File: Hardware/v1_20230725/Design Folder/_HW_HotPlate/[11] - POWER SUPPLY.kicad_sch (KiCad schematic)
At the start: 28 parts, among them U1101 MIC5528-3.3YMT-TR, U1102 MIC5528-3.3YMT-TR

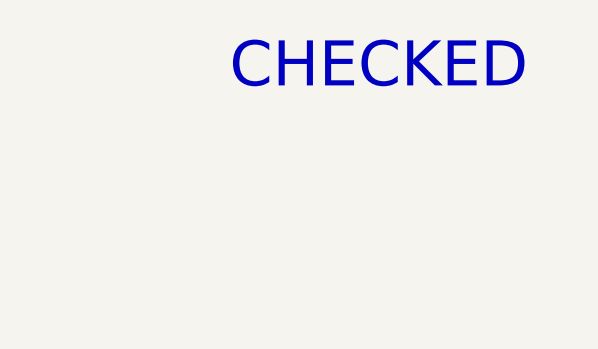
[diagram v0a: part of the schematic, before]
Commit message: Schematic library has been updated
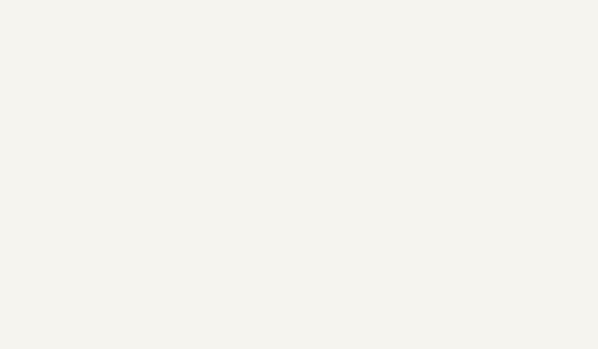
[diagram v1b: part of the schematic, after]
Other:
- note removed: "CHECKED"
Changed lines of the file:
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@@
 (kicad_sch (version 20230121) (generator eeschema)
-  (paper "B")
+  (paper "C")
   (title_block
     (title "Hot Plate")
@@
     (company "Mend0z0")
     (comment 1 "v1")
+    (comment 2 "RELEASED")
     (comment 3 "Siavash Taher Parvar")
     (comment 8 "N/A")
@@
     (effects (font (size 1.27 1.27)) (justify left bottom))
   )
-  (text "CHECKED" (at 382.27 35.56 0)
-    (effects (font (size 5 5)) (justify left bottom))
-  )
   (text "OUTPUT = 1A" (at 381 81.28 0)

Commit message: components have been updated
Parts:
- C1101: value 100nF/50V -> 100nF_50V_X7R; symbol _SCHLIB_HotPlate:CAP_100nF/50V_C0603 -> _SCHLIB_HotPlate:CAP_100nF_50V_X7R_C0603; Manufacturer (none) -> 1276-1000-2-ND; PCB CHECk (none) -> PCB (N/A); Part Number CL10B104KB8NNNC -> (none); Part Number (Manufacturer) (none) -> CL10B104KB8NNNC; Part Number (Vendor) (none) -> Samsung Electro-Mechanics; SCH CHECK CHECKED -> SCH (N/A); Vendor (none) -> Digikey
- C1102: symbol _SCHLIB_HotPlate:CAP_1nF/450V_C0805 -> _SCHLIB_HotPlate:CAP_1nF_450V_C0G_C0805; Manufacturer (none) -> 445-175679-2-ND; PCB CHECk (none) -> PCB (N/A); Part Number (Vendor) (none) -> TDK Corporation; SCH CHECK CHECKED -> SCH (N/A); Vendor (none) -> Digikey
- C1103, C1104, C1105, C1106: value 10uF/16V -> 10uF_16V_X5R; symbol _SCHLIB_HotPlate:CAP_10uF/16V-C0603 -> _SCHLIB_HotPlate:CAP_10uF_16V_X5R_C0603; Manufacturer (none) -> Murata Electronics; PCB CHECk (none) -> PCB (N/A); Part Number GRT188R61C106KE13J -> (none); Part Number (Manufacturer) (none) -> GRT188R61C106KE13J; Part Number (Vendor) (none) -> 490-GRT188R61C106KE13JTR-ND; SCH CHECK CHECKED -> SCH (N/A); Vendor (none) -> Digikey
- D1101: value SMBJ7.0A -> SMBJ7.0A_7V_50A; symbol _SCHLIB_HotPlate:TVS_SMBJ7.0A_SMB -> _SCHLIB_HotPlate:DIODE_TVS_SMBJ7.0A_7V_7.78V_50A(10/1000us)_SMB; Ipp 50A (10/1000 us) -> (none); Manufacturer (none) -> Bourns Inc.; PCB CHECk (none) -> PCB (N/A); Package (none) -> DO-214AA; Part Number SMBJ7.0A -> (none); Part Number (Manufacturer) (none) -> SMBJ7.0A; Part Number (Vendor) (none) -> SMBJ7.0ABTR-ND; SCH CHECK CHECKED -> SCH (N/A); VBR 7.78V (Vbr) -> (none); Vc 12V (Vc) -> (none); Vendor (none) -> Digikey
- EC1101: value 100uF/35V -> 100uF_35V_20%; symbol _SCHLIB_HotPlate:EC_100uF/35V_D66W77 -> _SCHLIB_HotPlate:CAP_ALUM_100uF_35V_20%_D66W77; Manufacturer (none) -> Cornell Dubilier Electronics (CDE); PCB CHECk (none) -> PCB (N/A); Part Number AFK107M35X16T-F -> (none); Part Number (Manufacturer) (none) -> AFK107M35X16T-F; Part Number (Vendor) (none) -> 338-2144-2-ND; SCH CHECK CHECKED -> SCH (N/A); Vendor (none) -> Digikey
- EC1102: value 10uF/400V -> 10uF_400V_20%; symbol _SCHLIB_HotPlate:ECAP_10uF/400V_L130W130 -> _SCHLIB_HotPlate:CAP_ALUM_10uF_400V_20%_L130W130; Manufacturer (none) -> Rubycon; PCB CHECk (none) -> PCB (N/A); Part Number 400SGV10M12.5X13.5 -> (none); Part Number (Manufacturer) (none) -> 400SGV10M12.5X13.5; Part Number (Vendor) (none) -> 1189-4102-2-ND; SCH CHECK CHECKED -> SCH (N/A); Vendor (none) -> Digikey
- L1101: value 50475C -> 4m7H_0.4A; symbol _SCHLIB_HotPlate:CMC_50475C -> _SCHLIB_HotPlate:IND_CMC_50475C_4.7mH_0.4A_0.7R_4 J-Lead; MAX CURRENT 0.4A -> (none); MAX DCR 0.7mR -> (none); Manufacturer (none) -> Murata Power Solutions Inc.; PCB CHECk (none) -> PCB (N/A); Package (none) -> 4 J-Lead; Part Number 50475C -> (none); Part Number (Manufacturer) (none) -> 50475C; Part Number (Vendor) (none) -> 811-1186-2-ND; SCH CHECK CHECKED -> SCH (N/A); Vendor (none) -> Digikey
- L1102: symbol _SCHLIB_HotPlate:IND_4.7uH_2.5A_L62W59 -> _SCHLIB_HotPlate:IND_4.7uH_2.5A_0.023R_N/A_L62W59; MAX DCR 23 mOhm (DCR) -> (none); Manufacturer (none) -> TDK Corporation; PCB CHECk (none) -> PCB (N/A); Part Number CLF6045T-4R7N-H -> (none); Part Number (Manufacturer) (none) -> CLF6045T-4R7N-H; Part Number (Vendor) (none) -> 445-15107-2-ND; SCH CHECK CHECKED -> SCH (N/A); Vendor (none) -> Digikey
- LED1101: value GREEN -> GREEN_2V8_0.02A; symbol _SCHLIB_HotPlate:LED_GREEN_0402 -> _SCHLIB_HotPlate:DIODE_LED_GREEN_2.8V_0.02A_522nm_LED0402; Manufacturer (none) -> Harvatek Corporation; PCB CHECk (none) -> PCB (N/A); Part Number B2841NG--05D000514U1930 -> (none); Part Number (Manufacturer) (none) -> B2841NG--05D000514U1930; Part Number (Vendor) (none) -> 3147-B2841NG--05D000514U1930TR-ND; SCH CHECK CHECKED -> SCH (N/A); VOLTAGE RATED 2V8 -> (none); Vendor (none) -> Digikey
- LED1102, LED1103: value AMBER -> AMBER_2V_0.02A; symbol _SCHLIB_HotPlate:LED_AMBER_0402 -> _SCHLIB_HotPlate:DIODE_LED_AMBER_2V_0.02A_592nm_LED0402; Manufacturer (none) -> Harvatek Corporation; PCB CHECk (none) -> PCB (N/A); Part Number B2841UY--20D000414U1930 -> (none); Part Number (Manufacturer) (none) -> B2841UY--20D000414U1930; Part Number (Vendor) (none) -> 3147-B2841UY--20D000414U1930TR-ND; SCH CHECK CHECKED -> SCH (N/A); VOLTAGE RATED 2V -> (none); Vendor (none) -> Digikey
- MOD1101: symbol _SCHLIB_HotPlate:PWS_LS05-13B05R3 -> _SCHLIB_HotPlate:IC_PWS_LS05-13B05R3_ACDC_85~305VAC_5V_1A_6-SIP Module; Manufacturer (none) -> Mornsun America, LLC; PCB CHECk (none) -> PCB (N/A); Package (none) -> 6-SIP Module; Part Number LS05-13B05R3 -> (none); Part Number (Manufacturer) (none) -> LS05-13B05R3; Part Number (Vendor) (none) -> 2725-LS05-13B05R3-ND; SCH CHECK CHECKED -> SCH (N/A); Vendor (none) -> Digikey
- R1101: value 15R_2W -> 15R_2W_5%; symbol _SCHLIB_HotPlate:RES_15R_2W_R2616 -> _SCHLIB_HotPlate:RES_15R_2W_5%_R2616; Manufacturer (none) -> TE Connectivity Passive Product; PCB CHECk (none) -> PCB (N/A); Part Number SMW215RJT -> (none); Part Number (Manufacturer) (none) -> SMW215RJT; Part Number (Vendor) (none) -> A103588TR-ND; SCH CHECK * -> SCH (N/A); Vendor (none) -> Digikey
- R1102, R1105, R1108: value 330R_1/10W -> 330R_1/10W_1%; symbol _SCHLIB_HotPlate:RES_330R_1/10W-R0402 -> _SCHLIB_HotPlate:RES_330R_1/10W_1%_R0402; Manufacturer (none) -> Panasonic Electronic Components; PCB CHECk (none) -> PCB (N/A); Part Number ERJ-2RKF3300X -> (none); Part Number (Manufacturer) (none) -> ERJ-2RKF3300X; Part Number (Vendor) (none) -> P330LTR-ND; SCH CHECK CHECKED -> SCH (N/A); Vendor (none) -> Digikey
- R1103, R1104, R1107: value 10KR_1/20W -> 10KR_1/20W_1%; symbol _SCHLIB_HotPlate:RES_10KR_1/20W-R0201 -> _SCHLIB_HotPlate:RES_10KR_1/20W_1%_R0201; Manufacturer (none) -> Stackpole Electronics Inc; PCB CHECk (none) -> PCB (N/A); Part Number RMCF0201FT10K0 -> (none); Part Number (Manufacturer) (none) -> RMCF0201FT10K0; Part Number (Vendor) (none) -> RMCF0201FT10K0TR-ND; SCH CHECK CHECKED -> SCH (N/A); Vendor (none) -> Digikey
- R1106: value 100R_1/20W -> 100R_1/20W_1%; symbol _SCHLIB_HotPlate:RES_100R_1/20W-R0201 -> _SCHLIB_HotPlate:RES_100R_1/20W_1%_R0201; Manufacturer (none) -> Stackpole Electronics Inc; PCB CHECk (none) -> PCB (N/A); Part Number RMCF0201FT100R -> (none); Part Number (Manufacturer) (none) -> RMCF0201FT100R; Part Number (Vendor) (none) -> RMCF0201FT100RTR-ND; SCH CHECK CHECKED -> SCH (N/A); Vendor (none) -> Digikey
- RV1101: value B72214P2351K101 -> B72214P2351K101_350VAC_6kA; symbol _SCHLIB_HotPlate:MOV_B72214P2351K101_D170P75 -> _SCHLIB_HotPlate:VDR_MOV_B72214P2351K101_350VAC_460VDC_6kA_D170P75; Manufacturer (none) -> EPCOS - TDK Electronics; PCB CHECk (none) -> PCB (N/A); Part Number B72214P2351K101 -> (none); Part Number (Manufacturer) (none) -> B72214P2351K101; Part Number (Vendor) (none) -> 495-B72214P2351K101-ND; SCH CHECK CHECKED -> SCH (N/A); Vendor (none) -> Digikey
- TC1101, TC1102: value 220uF/16V -> 220uF_16V_0.7R; symbol _SCHLIB_HotPlate:TCAP_220uF/16V_Size N -> _SCHLIB_HotPlate:CAP_TANT_220uF_16V_0.7R_Size N; Manufacturer (none) -> KYOCERA AVX; PCB CHECk (none) -> PCB (N/A); Package Size N -> C2917; Part Number F931C227MNC -> (none); Part Number (Manufacturer) (none) -> F931C227MNC; Part Number (Vendor) (none) -> 478-8258-2-ND; SCH CHECK CHECKED -> SCH (N/A); Vendor (none) -> Digikey
- U1101, U1102: symbol _SCHLIB_HotPlate:PMIC_MIC5528-3.3YMT-TR -> _SCHLIB_HotPlate:IC_PMIC_MIC5528-3.3YMT-TR_LDO_3.3V_0.5A_6-TDFN (1.2x1.2); Manufacturer (none) -> Microchip Technology; PCB CHECk (none) -> PCB (N/A); Package (none) -> 6-TDFN (1.2x1.2); Part Number MIC5528-3.3YMT-TR -> (none); Part Number (Manufacturer) (none) -> MIC5528-3.3YMT-TR; Part Number (Vendor) (none) -> 576-4766-2-ND; SCH CHECK CHECKED -> SCH (N/A); Vendor (none) -> Digikey
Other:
- moved on the sheet: C1101, C1102, C1103, C1104, C1105, C1106, D1101, EC1101, EC1102, L1101, L1102, LED1101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
